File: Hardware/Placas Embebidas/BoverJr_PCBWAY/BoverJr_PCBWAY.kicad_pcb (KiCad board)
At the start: 2 copper layers, 100 x 100 mm, 39 parts, among them J1 Encoder Derecho, J10 7.4v, J2 Encoder Izquierdo, J3 Programador, J4 Distancia_Der, J5 Distancia_Izq, J8 Distancia_Frontal, SW1 SW_SPDT, U1 ESP32-WROOM-32E, U2 MPU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

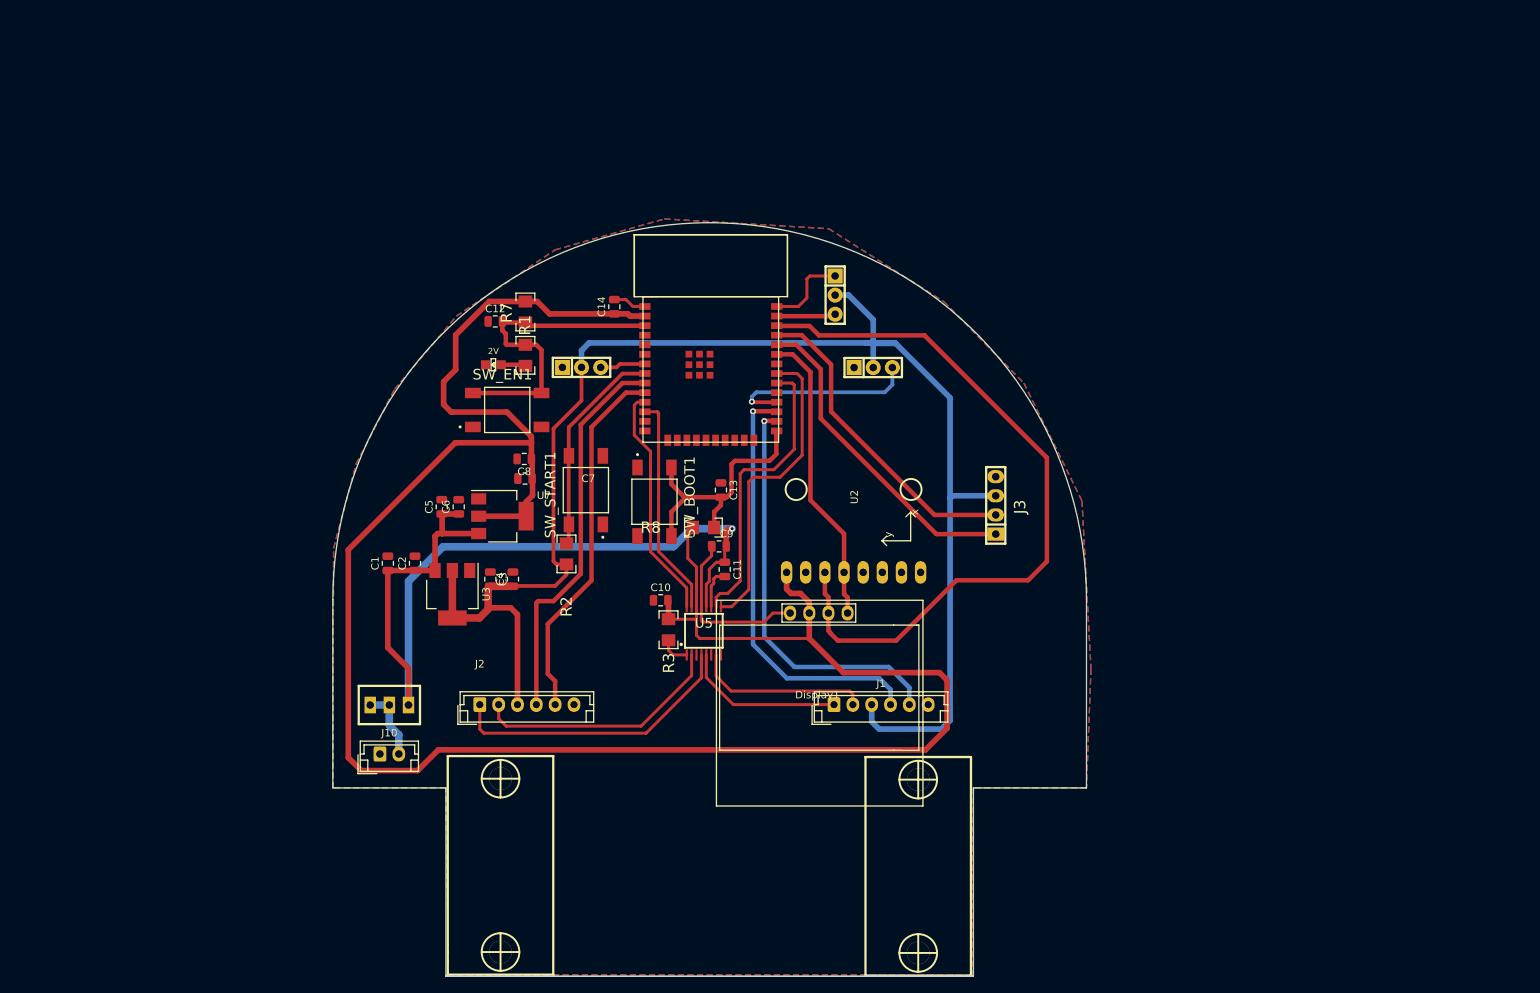
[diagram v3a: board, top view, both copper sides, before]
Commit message: agregue logos , acomode serigrafia y componentes , agregue pads
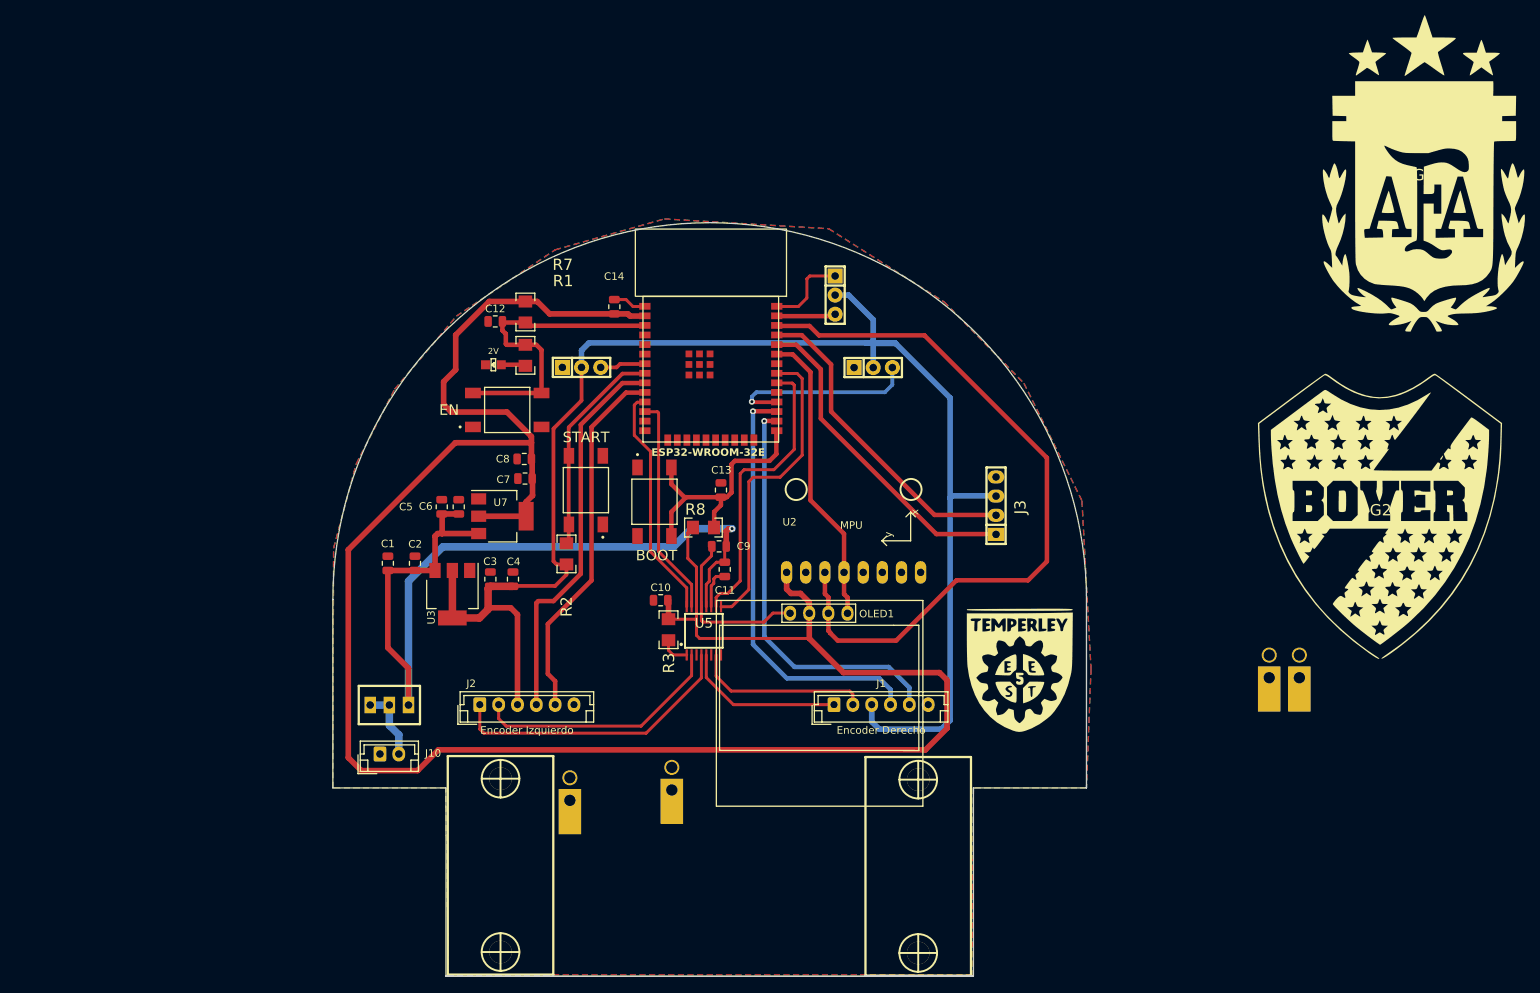
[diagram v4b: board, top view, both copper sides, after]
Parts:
- removed Display1: SSD1306-SSD1306-128x64_OLED, EESTN5:128x64OLED
- added G1: LOGO_EESTN5_2, EESTN5:EESTN5, F.Cu at (191.2, 89.2)
- added G2: LOGO, EESTN5:Bover_huella_frontal, F.Cu at (239.0, 67.9)
- added G3: LOGO, EESTN5:AFA, F.Cu at (244.7, 23.5)
- added J11: Cable_PAD, EESTN5:Cable_Doble_1,5mm, F.Cu at (131.4, 106.5)
- added J6: Cable_PAD, EESTN5:Cable_Doble_1,5mm, F.Cu at (224.2, 90.2)
- added J7: Cable_PAD, EESTN5:Cable_Doble_1,5mm, F.Cu at (228.2, 90.2)
- added J9: Cable_PAD, EESTN5:Cable_Doble_1,5mm, F.Cu at (145.0, 105.1)
- added OLED1: SSD1306-SSD1306-128x64_OLED, EESTN5:128x64OLED, F.Cu at (164.3, 92.2)
- H1: value MOTOR_IZQ -> Soporte_Motor_IZQ
- H2: value MOTOR_DER -> Soporte_Motor_DER
- J10: value 7.4v -> 2s
- U1: footprint ESP32-WROOM-32E:ESP32-WROOM-32E -> EESTN5:ESP32-WROOM-32E
- moved J3 0.06 mm to (188.0, 67.3)
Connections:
- U1 pad 10: /OUT_M2_DB -> unconnected-(U1-IO34-Pad10)
- U1 pad 11: /M2_IN1 -> /IR_DER
- U1 pad 12: /M2_IN2 -> /START
- U1 pad 13: unconnected-(U1-IO14-Pad13) -> /OUT_M2_DA
- U1 pad 14: unconnected-(U1-IO12-Pad14) -> /OUT_M2_DB
- U1 pad 15: GND -> /M2_IN1
- U1 pad 16: unconnected-(U1-IO13-Pad16) -> /M2_IN2
- U1 pad 23: unconnected-(U1-IO15-Pad23) -> /BOOT
- U1 pad 24: unconnected-(U1-IO2-Pad24) -> /OUT_M1_DB
- U1 pad 25: /BOOT -> /OUT_M1_DA
- U1 pad 27: /OUT_M1_DA -> /IR_IZQ
- U1 pad 28: /IR_IZQ -> unconnected-(U1-SD2-Pad28)
- U1 pad 30: /M1_IN2 -> unconnected-(U1-CMD-Pad30)
- U1 pad 31: /M1_IN1 -> unconnected-(U1-CLK-Pad31)
- U1 pad 33: /SDA -> unconnected-(U1-SD1-Pad33)
- U1 pad 34: /RX -> unconnected-(U1-IO5-Pad34)
- U1 pad 35: /TX -> /M1_IN2
- U1 pad 36: /SCL -> /IR_FRONTAL
- U1 pad 38: GND -> /M1_IN1
- U1 pad 8: /START -> unconnected-(U1-SENSOR_VN-Pad8)
- U1 pad 9: /OUT_M2_DA -> /EN

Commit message: acomode pads y quedo casi lista falta verificar por 3d
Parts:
- J10: value 2s -> 7.4v
- J9: moved to B.Cu
- moved J6 73.1 mm to (152.4, 103.6)
- moved J7 72.6 mm to (156.9, 103.6)
- moved J11 16.3 mm to (147.5, 103.7)
- moved J10 5.06 mm to (105.0, 95.4)
- moved H2 5.03 mm to (172.7, 115.2)
- moved H1 4.85 mm to (127.1, 115.2)
- moved SW1 4.24 mm to (108.9, 89.8)
- moved J9 2.47 mm to (143.0, 103.6), turned to 180 degrees
- turned J4 to 180 degrees
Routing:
- net /OUT_B_MOTOR2: track 33.4 -> 69.6 mm
- net /OUT_A_MOTOR2: track 39.0 -> 68.9 mm
- net /OUT_A_MOTOR1: track 21.4 -> 43.8 mm
- net /OUT_B_MOTOR1: track 23.3 -> 43.8 mm
- net VCC: track 115.8 -> 106.5 mm
- net +3.3V: track 283.6 -> 278.1 mm
- net /IR_IZQ: track 25.6 -> 20.7 mm
- net +BATT: track 9.56 -> 8.72 mm
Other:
- board size 100 x 100 mm -> 100 x 100.1 mm

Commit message: estoy verificando por 3d
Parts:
- added G6: LOGO, EESTN5:BOVER_NAME, F.Cu at (174.3, 56.0)
- G2: footprint EESTN5:Bover_huella_frontal -> EESTN5:Bover_Huella_frontal_FCU
- moved G2 110.7 mm to (128.4, 64.5)
- moved G3 83.9 mm to (171.2, 63.9)
- moved G1 4.78 mm to (190.9, 94.0)
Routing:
- net VCC: track 106.5 -> 102.2 mm
- net /OUT_M2_DB: track 48.6 -> 47.9 mm
- net /OUT_M2_DA: track 51.6 -> 51.0 mm
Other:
- board text added: "LEANDRO BENITEZ EZEQUIEL SIERRA"

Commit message: soy un boludo
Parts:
- moved H2 0.30 mm to (172.9, 115.3)
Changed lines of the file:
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@@
   )
   (footprint "EESTN5:Pololu_Micro_Con_Soporte_Simple" (layer "F.Cu")
-    (at 172.65 115.25 90)
+    (at 172.95 115.3 90)
     (descr "Pololu Micro Gear Motor W/Mount")
     (property "Sheetfile" "BoverJr_PCBWAY.kicad_sch")
@@
     (pad "3" thru_hole rect (at 2.54 0) (size 1.524 2.19964) (drill 1.00076) (layers "*.Cu" "*.Mask" "F.SilkS")
       (net 15 "VCC") (pinfunction "C") (pintype "passive"))
-    (model "SW-SPDT-TH-100Mils-Vertical.wrl"
+    (model "C:/Users/juana/Dropbox/GIT/Librerias-Kicad/EESTN5.3dshapes/SW-SPDT-TH-100Mils-Vertical.wrl"
       (offset (xyz 0 0 0))
       (scale (xyz 1 1 1))
@@
     (polygon
       (pts
-        (xy 200.055689 129.799902)
-        (xy 199.855689 29.699902)
-        (xy 99.655689 29.699902)
-        (xy 99.955689 129.899902)
+        (xy 180 129.9)
+        (xy 120 129.8)
+        (xy 120 102.9)
+        (xy 100 102.9)
+        (xy 100 75.7)
+        (xy 101.55 66.7)
+        (xy 104.9 58.1)
+        (xy 108.35 51.85)
+        (xy 112.9 46.25)
+        (xy 116.55 42.55)
+        (xy 120.95 39)
+        (xy 126.85 35.4)
+        (xy 134.15 32.2)
+        (xy 140.15 30.655)
+        (xy 147.35 29.75)
+        (xy 154.6 29.75)
+        (xy 160.16 30.625)
+        (xy 168.45 33.2)
+        (xy 175.2 36.5)
+        (xy 181.7 41.1)
+        (xy 186.85 45.9)
+        (xy 191.4 51.65)
+        (xy 195.35 58.5)
+        (xy 198.6 67.55)
+        (xy 199.9 75.65)
+        (xy 200.05 87.8)
+        (xy 200.05 102.9)
+        (xy 180 102.9)
       )
     )

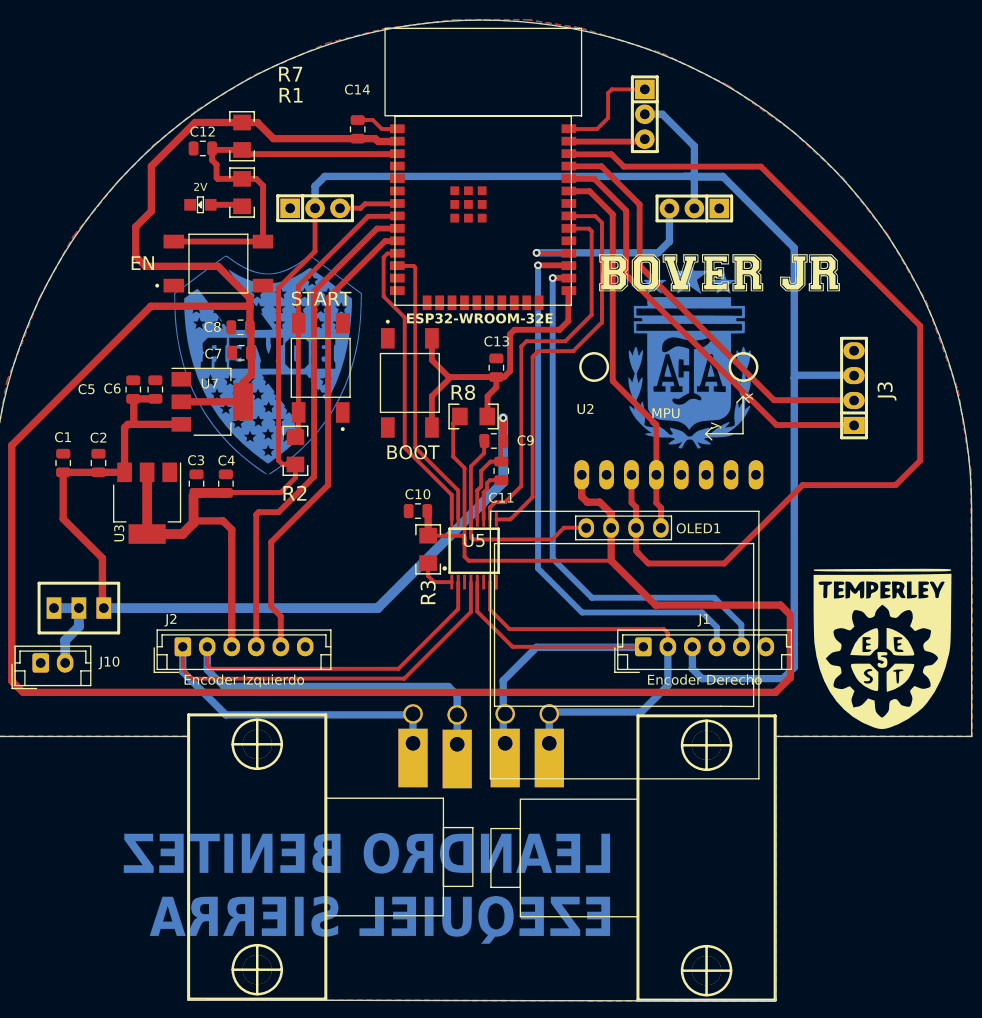
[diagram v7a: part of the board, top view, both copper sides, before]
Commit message: correccion de algunas pistas
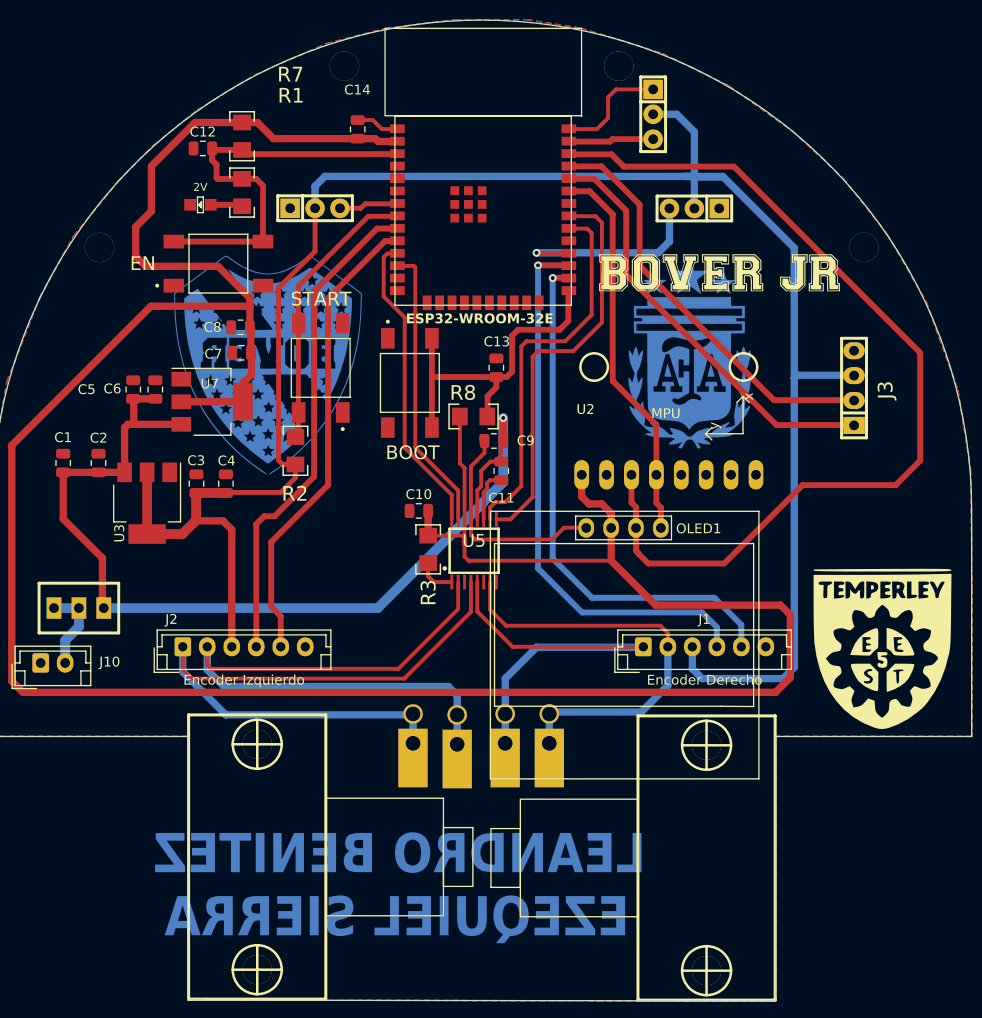
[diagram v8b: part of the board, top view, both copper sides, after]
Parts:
- added ?: , , F.Cu at (111.0, 53.0)
- added ?: , , F.Cu at (136.0, 34.5)
- added ?: , , F.Cu at (189.0, 53.0)
- added ?: , , F.Cu at (164.0, 34.5)
- moved J8 0.85 mm to (167.5, 39.4)
- moved C10 0.09 mm to (143.6, 79.9)
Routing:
- net /SCL: track 98.7 -> 97.1 mm
- net /IR_FRONTAL: track 7.86 -> 8.71 mm
- net /OUT_M2_DA: track 51.0 -> 50.5 mm
- net +3.3V: track 278.1 -> 277.6 mm
